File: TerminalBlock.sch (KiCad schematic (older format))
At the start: 2 parts, among them P4 12 Pin Terminal Block, P5 3 Pin TB

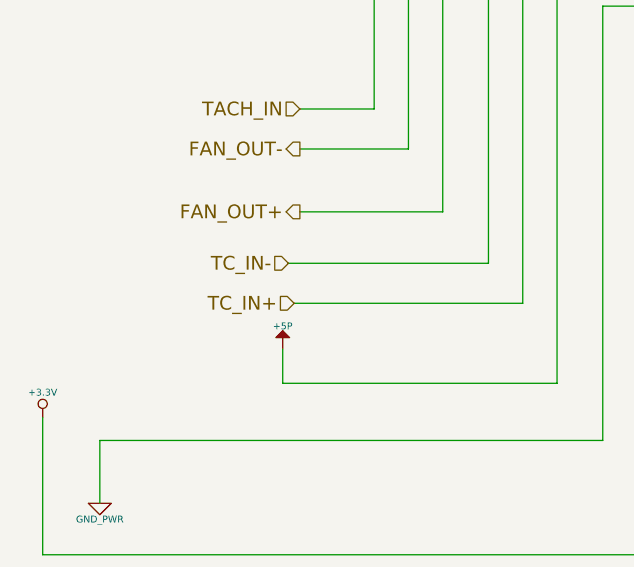
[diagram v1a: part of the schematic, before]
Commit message: Layout Work Session 12
Pulled from CE.

Session 11 missed due to corrupted pcb file pulled from CE
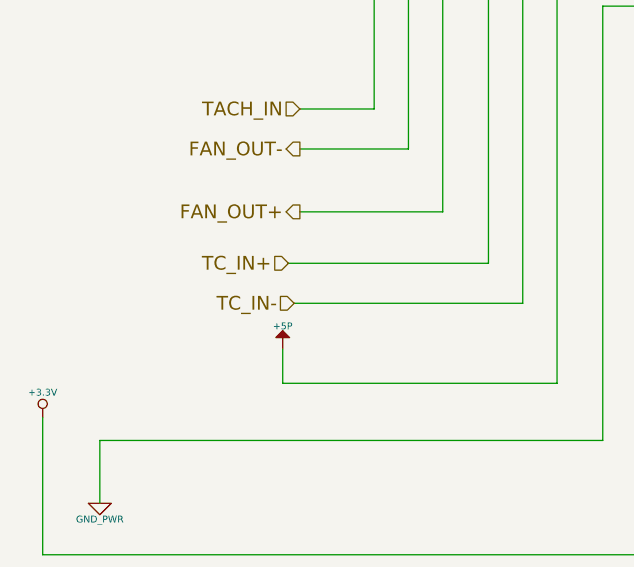
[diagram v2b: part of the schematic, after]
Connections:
- net TC_IN+: now also P4.6 (P6); no longer P4.7 (P7)
- net TC_IN-: now also P4.7 (P7); no longer P4.6 (P6)
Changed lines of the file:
@@
-EESchema Schematic File Version 2
+EESchema Schematic File Version 2  date 11/21/2013 11:46:41 PM
 LIBS:power
 LIBS:device
@@
 LIBS:BenchBuddy
 LIBS:BenchBuddy-cache
-EELAYER 24 0
+EELAYER 27 0
 EELAYER END
 $Descr A4 11693 8268
@@
 Sheet 7 9
 Title ""
-Date "13 nov 2013"
+Date "22 nov 2013"
 Rev ""
 Comp ""
@@
 Text HLabel 1425 1350 0    60   Output ~ 0
 LED_STRING-
+Text HLabel 1825 2825 0    60   Input ~ 0
+TC_IN+
 Text HLabel 1850 3000 0    60   Input ~ 0
-TC_IN+
-Text HLabel 1825 2825 0    60   Input ~ 0
 TC_IN-
 Text HLabel 2850 5500 0    60   BiDi ~ 0
@@
 RELAY_NC
 $Comp
-L +3.3V #PWR038
+L +3.3V #PWR037
 U 1 1 523FFDA7
 P 750 3500
-F 0 "#PWR038" H 750 3460 30  0001 C CNN
+F 0 "#PWR037" H 750 3460 30  0001 C CNN
 F 1 "+3.3V" H 750 3610 30  0000 C CNN
 F 2 "~" H 750 3500 60  0000 C CNN
@@
 	1450 900  5500 900
 $Comp
-L GND_PWR #PWR039
+L GND_PWR #PWR038
 U 1 1 527EF77D
 P 1000 3875
-F 0 "#PWR039" H 1000 3875 30  0001 C CNN
+F 0 "#PWR038" H 1000 3875 30  0001 C CNN
 F 1 "GND_PWR" H 1000 3805 30  0000 C CNN
 F 2 "~" H 1000 3875 60  0000 C CNN
@@
 	1800 3200 1800 3350
 $Comp
-L +5P #PWR46
+L +5P #PWR45
 U 1 1 52831A41
 P 1800 3200
-F 0 "#PWR46" H 1800 3330 20  0001 C CNN
+F 0 "#PWR45" H 1800 3330 20  0001 C CNN
 F 1 "+5P" H 1800 3300 30  0000 C CNN
 F 2 "~" H 1800 3200 60  0000 C CNN
